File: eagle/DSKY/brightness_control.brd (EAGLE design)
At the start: 12 parts, among them IC101 NE555V, T101 NX2301P, T102 NX2301P

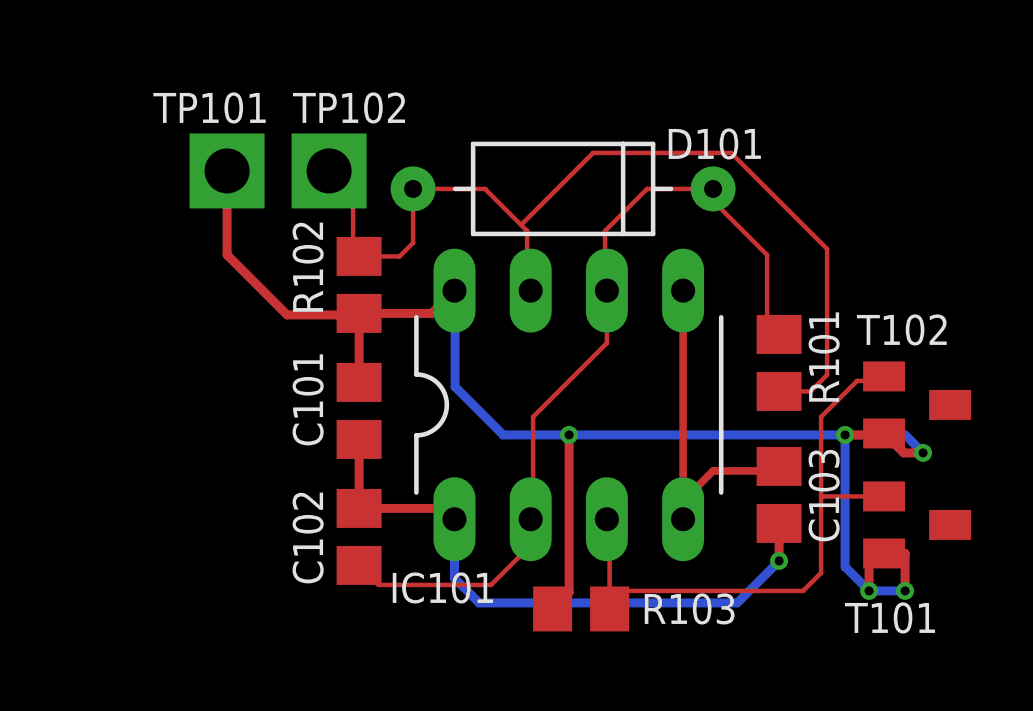
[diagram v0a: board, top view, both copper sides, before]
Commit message: reverse voltage protection
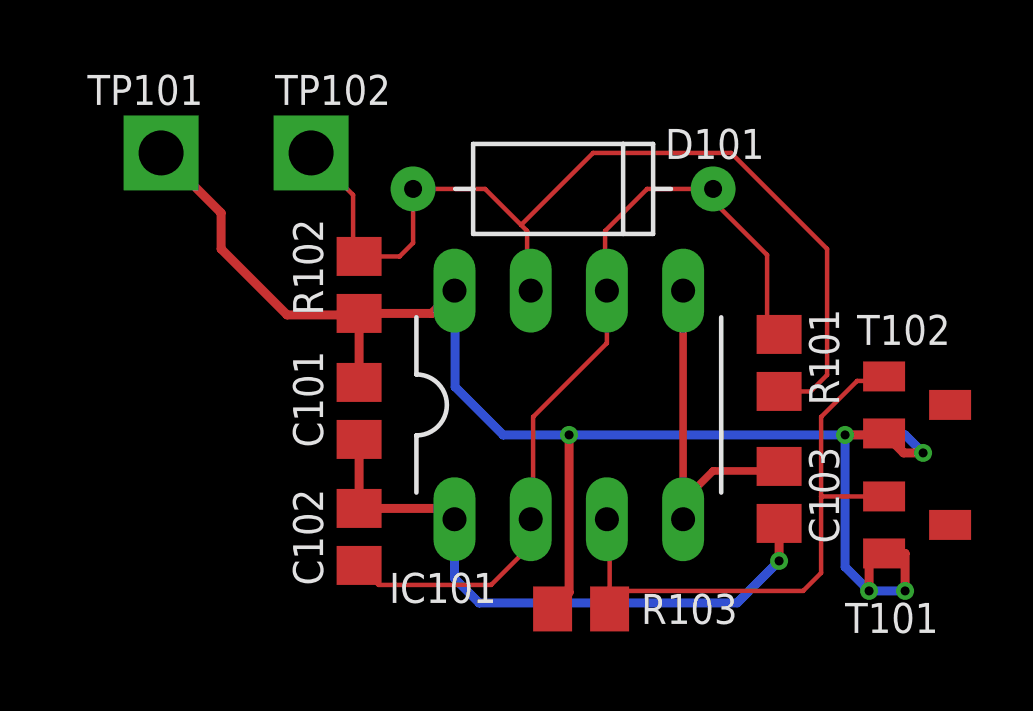
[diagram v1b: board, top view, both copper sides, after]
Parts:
- moved TP101 2.28 mm to (0.00, 19.0)
- moved TP102 0.85 mm to (5.00, 19.0)
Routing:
- net P5V: track 53.0 -> 54.5 mm
- net TIM_3: track 32.0 -> 32.9 mm
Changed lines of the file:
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@@
 <setting verticaltext="up"/>
 </settings>
-<grid distance="0.2" unitdist="mm" unit="mm" style="lines" multiple="1" display="no" altdistance="0.2" altunitdist="mm" altunit="mm"/>
+<grid distance="1" unitdist="mm" unit="mm" style="lines" multiple="1" display="yes" altdistance="0.2" altunitdist="mm" altunit="mm"/>
 <layers>
 <layer number="1" name="Top" color="4" fill="1" visible="yes" active="yes"/>
@@
 <attribute name="VALUE" x="10.669" y="9.965" size="1" layer="27" font="vector" ratio="13"/>
 </element>
-<element name="TP102" library="be_con_jump" package="T_TEST_POINT_LARGE" value="" x="5.6" y="18.4" smashed="yes">
-<attribute name="UPDATED" value="" x="33.54" y="4.43" size="1.778" layer="27" display="off"/>
-<attribute name="PART_CODE_EXT" value="" x="33.54" y="4.43" size="1.778" layer="27" display="off"/>
-<attribute name="FUNCTION" value="" x="33.54" y="4.43" size="1.778" layer="27" display="off"/>
-<attribute name="COMMISSIONED" value="2014-09-03" x="33.54" y="4.43" size="1.778" layer="27" display="off"/>
-<attribute name="PART_CODE_BEL" value="TP_PAC_T_TEST_POINT_SMALL" x="33.54" y="4.43" size="1.778" layer="27" display="off"/>
-<attribute name="BOM" value="NO" x="33.54" y="4.43" size="1.778" layer="27" display="off"/>
-<attribute name="NAME" x="4.4" y="20" size="1" layer="25" font="vector" ratio="13"/>
-<attribute name="VALUE" x="4.1" y="19.9" size="1" layer="27" font="vector" ratio="13"/>
-</element>
-<element name="TP101" library="be_con_jump" package="T_TEST_POINT_LARGE" value="" x="2.2" y="18.4" smashed="yes">
-<attribute name="UPDATED" value="" x="33.95" y="4.43" size="1.778" layer="27" display="off"/>
-<attribute name="PART_CODE_EXT" value="" x="33.95" y="4.43" size="1.778" layer="27" display="off"/>
-<attribute name="FUNCTION" value="" x="33.95" y="4.43" size="1.778" layer="27" display="off"/>
-<attribute name="COMMISSIONED" value="2014-09-03" x="33.95" y="4.43" size="1.778" layer="27" display="off"/>
-<attribute name="PART_CODE_BEL" value="TP_PAC_T_TEST_POINT_SMALL" x="33.95" y="4.43" size="1.778" layer="27" display="off"/>
-<attribute name="BOM" value="NO" x="33.95" y="4.43" size="1.778" layer="27" display="off"/>
-<attribute name="NAME" x="3.6" y="21" size="1" layer="25" font="vector" ratio="13" rot="R180"/>
-<attribute name="VALUE" x="0.7" y="19.9" size="1" layer="27" font="vector" ratio="13"/>
+<element name="TP102" library="be_con_jump" package="T_TEST_POINT_LARGE" value="" x="5" y="19" smashed="yes">
+<attribute name="UPDATED" value="" x="32.94" y="5.03" size="1.778" layer="27" display="off"/>
+<attribute name="PART_CODE_EXT" value="" x="32.94" y="5.03" size="1.778" layer="27" display="off"/>
+<attribute name="FUNCTION" value="" x="32.94" y="5.03" size="1.778" layer="27" display="off"/>
+<attribute name="COMMISSIONED" value="2014-09-03" x="32.94" y="5.03" size="1.778" layer="27" display="off"/>
+<attribute name="PART_CODE_BEL" value="TP_PAC_T_TEST_POINT_SMALL" x="32.94" y="5.03" size="1.778" layer="27" display="off"/>
+<attribute name="BOM" value="NO" x="32.94" y="5.03" size="1.778" layer="27" display="off"/>
+<attribute name="NAME" x="3.8" y="20.6" size="1" layer="25" font="vector" ratio="13"/>
+<attribute name="VALUE" x="3.5" y="20.5" size="1" layer="27" font="vector" ratio="13"/>
+</element>
+<element name="TP101" library="be_con_jump" package="T_TEST_POINT_LARGE" value="" x="0" y="19" smashed="yes">
+<attribute name="UPDATED" value="" x="31.75" y="5.03" size="1.778" layer="27" display="off"/>
+<attribute name="PART_CODE_EXT" value="" x="31.75" y="5.03" size="1.778" layer="27" display="off"/>
+<attribute name="FUNCTION" value="" x="31.75" y="5.03" size="1.778" layer="27" display="off"/>
+<attribute name="COMMISSIONED" value="2014-09-03" x="31.75" y="5.03" size="1.778" layer="27" display="off"/>
+<attribute name="PART_CODE_BEL" value="TP_PAC_T_TEST_POINT_SMALL" x="31.75" y="5.03" size="1.778" layer="27" display="off"/>
+<attribute name="BOM" value="NO" x="31.75" y="5.03" size="1.778" layer="27" display="off"/>
+<attribute name="NAME" x="1.4" y="21.6" size="1" layer="25" font="vector" ratio="13" rot="R180"/>
+<attribute name="VALUE" x="-1.5" y="20.5" size="1" layer="27" font="vector" ratio="13"/>
 </element>
 <element name="D101" library="be_diode" package="T_DO204_GRID_10MM" value="BAT48" x="13.4" y="17.8" smashed="yes">
@@
 <wire x1="7.95" y1="15.55" x2="8.4" y2="16" width="0.15" layer="1"/>
 <wire x1="8.4" y1="16" x2="8.4" y2="17.8" width="0.15" layer="1"/>
-<wire x1="5.6" y1="18.4" x2="6.4" y2="17.6" width="0.15" layer="1"/>
+<wire x1="5" y1="19" x2="6.4" y2="17.6" width="0.15" layer="1"/>
 <wire x1="6.4" y1="17.6" x2="6.4" y2="15.75" width="0.15" layer="1"/>
 <wire x1="6.4" y1="15.75" x2="6.6" y2="15.55" width="0.15" layer="1"/>
@@
 <wire x1="9.8" y1="14.39" x2="9.78" y2="14.41" width="0.3" layer="16"/>
 <contactref element="C101" pad="1"/>
-<wire x1="2.2" y1="18.4" x2="2.2" y2="15.6" width="0.3" layer="1"/>
-<wire x1="2.2" y1="15.6" x2="4.2" y2="13.6" width="0.3" layer="1"/>
+<wire x1="2" y1="15.8" x2="4.2" y2="13.6" width="0.3" layer="1"/>
 <wire x1="4.2" y1="13.6" x2="6.55" y2="13.6" width="0.3" layer="1"/>
 <wire x1="6.55" y1="13.6" x2="6.6" y2="13.65" width="0.3" layer="1"/>
@@
 <wire x1="13.6" y1="4.35" x2="13.6" y2="9.6" width="0.3" layer="1"/>
 <via x="13.6" y="9.6" extent="1-16" drill="0.3"/>
+<wire x1="2" y1="15.8" x2="2" y2="17" width="0.3" layer="1"/>
+<wire x1="2" y1="17" x2="0" y2="19" width="0.3" layer="1"/>
 </signal>
 <signal name="P5V_PWM1">
